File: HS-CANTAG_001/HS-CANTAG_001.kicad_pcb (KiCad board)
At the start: 2 copper layers, 81.3 x 52.1 mm, 28 parts, among them J1 B2B-PH-K-S_LF__SN_, J2 B4B-XH-A_LF__SN_, J3 Barrel_Jack, J4 CAN1, J5 CAN2, SW1 SW_Push, U1 MCP2515, U2 R-78E5.0-0.5, U3 MCP2551, Y1 16MHz

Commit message: ・回路修正
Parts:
- J4, J5: footprint Connector_Hirose:Hirose_DF63-4P-3.96DSA_1x04_P3.96mm_Horizontal -> Connector_JST:JST_VH_B4P-VH_1x04_P3.96mm_Vertical
- moved C1 77.4 mm to (134.5, 98.5)
- moved C2 77.4 mm to (156.1, 88.6)
- moved C3 77.4 mm to (149.8, 117.6)
- moved C4 77.4 mm to (159.9, 117.6)
- moved C5 77.4 mm to (172.6, 122.7)
- moved C6 77.4 mm to (123.1, 110.0)
- moved C7 77.4 mm to (130.7, 102.4)
- moved C8 77.4 mm to (130.7, 94.7)
- moved C9 77.4 mm to (123.1, 87.2)
- moved CAN_H1 77.4 mm to (170.1, 82.1)
- moved D1 77.4 mm to (162.5, 89.7)
- moved D2 77.4 mm to (132.0, 115.1)
- moved J1 77.4 mm to (132.0, 80.8)
- moved J2 77.4 mm to (142.0, 80.9)
- moved J3 77.4 mm to (120.6, 120.2)
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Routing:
- net Net-(U1-Pad1): track 0.00 -> 41.2 mm
- net Net-(U1-Pad2): track 0.00 -> 26.9 mm
- net +5V: track 225.2 -> 234.0 mm
- net Net-(CAN_H1-Pad2): track 69.7 -> 78.5 mm
- added copper zone on B.Cu, net GNDPWR
- added copper zone on F.Cu, net GNDPWR
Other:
- outline, holes or cut-outs redrawn

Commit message: ・CAN回路更新
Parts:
- U1: value MCP2515 -> MCP2515_SMD18p; footprint hotsprings-footprints:MCP2515_SMD -> hotsprings-footprints:MCP2515_SMD(18p)
- moved U1 1.28 mm to (154.9, 104.1)
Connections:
- U1 pad 10: GNDPWR -> Net-(U1-Pad10)
- U1 pad 11: Net-(U1-Pad11) -> Net-(D1-Pad2)
- U1 pad 12: Net-(D1-Pad2) -> Net-(U1-Pad12)
- U1 pad 13: Net-(U1-Pad13) -> Net-(J2-Pad1)
- U1 pad 14: Net-(J2-Pad1) -> Net-(J2-Pad2)
- U1 pad 15: Net-(U1-Pad15) -> Net-(J2-Pad3)
- U1 pad 16: Net-(J2-Pad2) -> Net-(J2-Pad4)
- U1 pad 17: Net-(J2-Pad3) -> Net-(R1-Pad2)
- U1 pad 18: Net-(J2-Pad4) -> +5V
- U1 pad 7: Net-(U1-Pad7) -> Net-(C3-Pad1)
- U1 pad 8: Net-(C3-Pad1) -> Net-(C4-Pad1)
- U1 pad 9: Net-(C4-Pad1) -> GNDPWR
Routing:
- net Net-(U1-Pad2): track 26.9 -> 33.0 mm
- net +5V: track 234.0 -> 229.3 mm
- net Net-(U1-Pad1): track 41.2 -> 37.3 mm
- net Net-(C3-Pad1): track 22.8 -> 20.2 mm
- net Net-(J2-Pad3): track 30.3 -> 28.1 mm
- net Net-(C4-Pad1): track 18.4 -> 16.3 mm
- net Net-(J2-Pad1): track 40.2 -> 38.3 mm
- net Net-(J2-Pad2): track 35.4 -> 33.5 mm
- net Net-(R1-Pad2): track 17.8 -> 16.0 mm
- net Net-(J2-Pad4): track 22.2 -> 20.9 mm
- net Net-(D1-Pad2): track 12.7 -> 11.5 mm

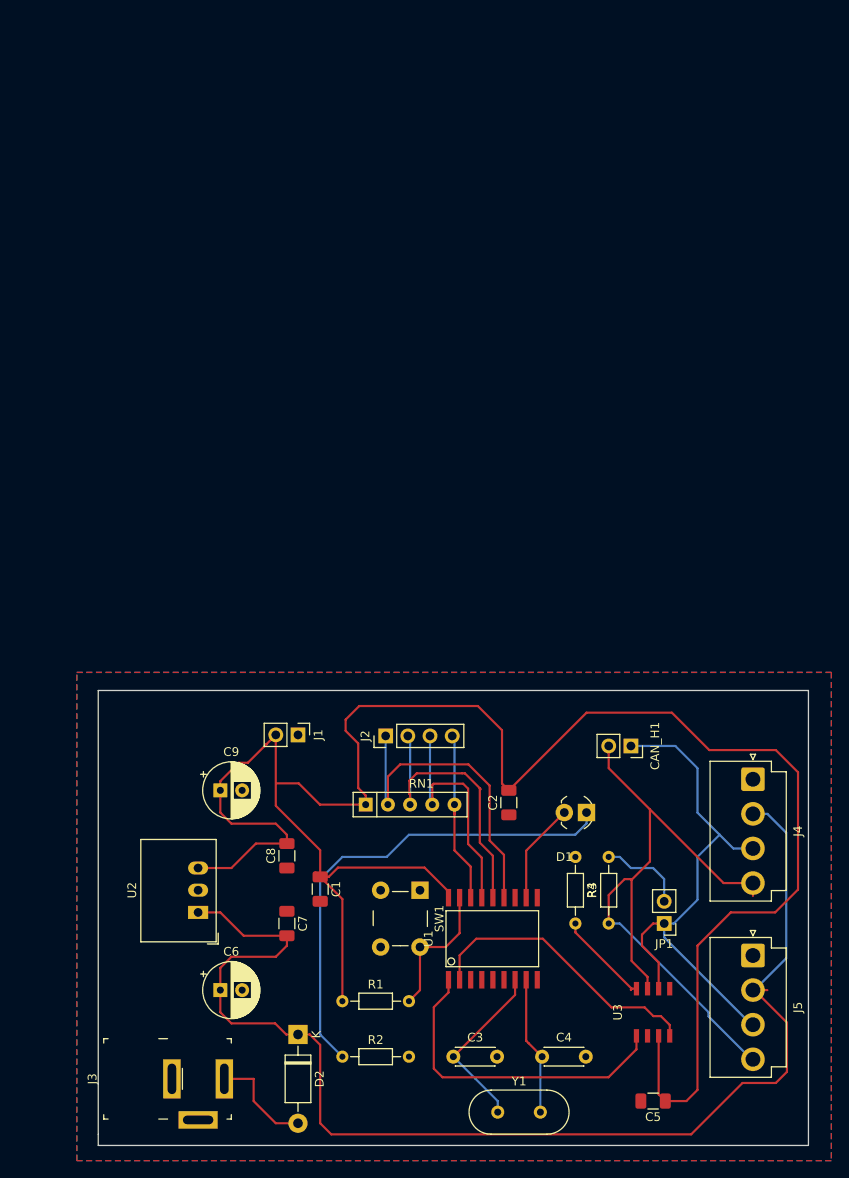
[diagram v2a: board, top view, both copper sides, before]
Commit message: ・CANTAG外形データの追加
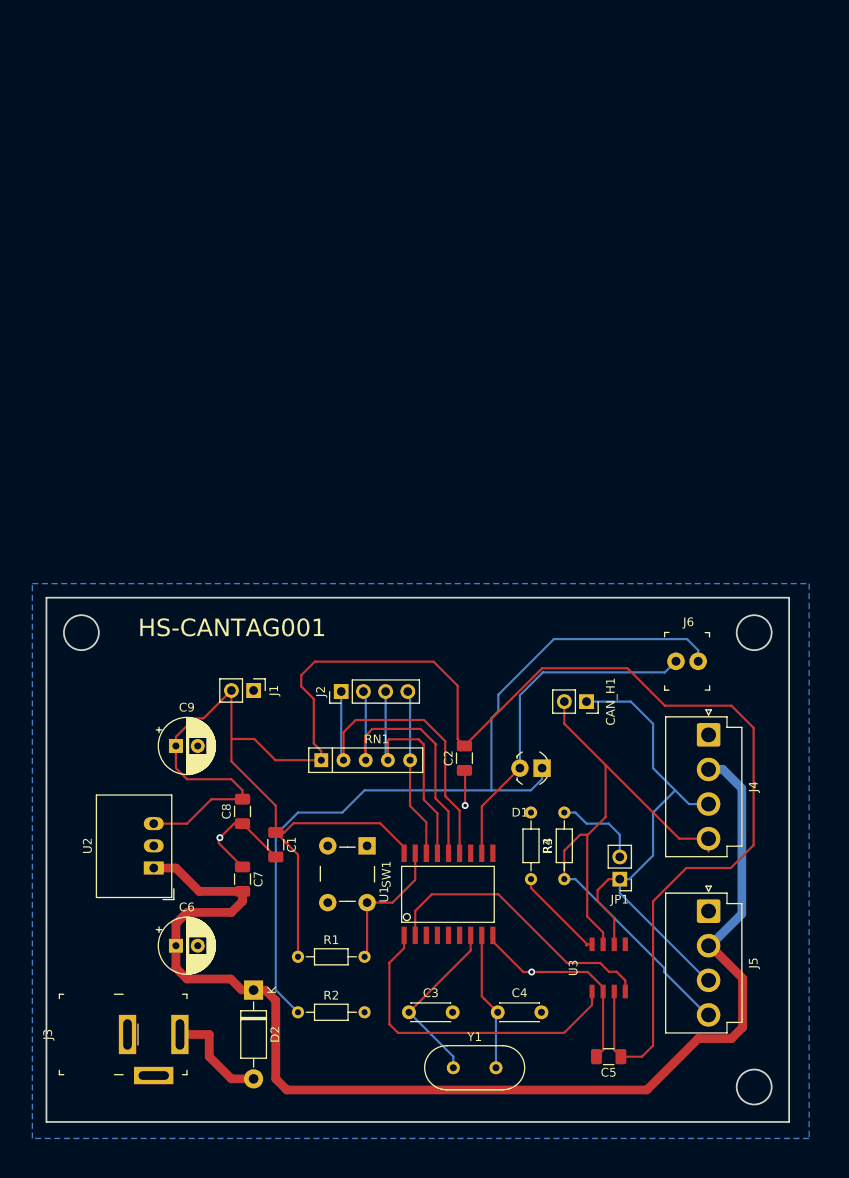
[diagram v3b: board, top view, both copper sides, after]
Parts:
- added J6: 640456-2, digikey-footprints:PinHeader_1x2_P2.54mm_Drill1.02mm, F.Cu at (175.3, 72.4)
- moved SW1 7.90 mm to (139.9, 93.5)
- moved J2 7.18 mm to (136.9, 75.8)
- moved R1 7.18 mm to (132.0, 106.2)
- moved R4 7.18 mm to (162.5, 97.3)
- moved RN1 7.18 mm to (134.7, 83.7)
- moved C3 7.18 mm to (144.7, 112.6)
- moved J3 7.18 mm to (115.5, 115.1)
- moved R2 7.18 mm to (132.0, 112.6)
- moved R3 7.18 mm to (158.7, 89.7)
- moved Y1 7.18 mm to (149.8, 118.9)
- moved C6 7.18 mm to (118.0, 104.9)
- moved C7 7.18 mm to (125.7, 97.3)
- moved C8 7.18 mm to (125.7, 89.6)
- moved C9 7.18 mm to (118.0, 82.1)
- moved D2 7.18 mm to (126.9, 110.0)
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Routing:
- net GNDPWR: track 0.00 -> 41.0 mm, vias 0 -> 3
- net Net-(D1-Pad1): track 55.7 -> 94.3 mm
- net Net-(D1-Pad2): track 11.5 -> 39.4 mm
- net VCC: track 142.1 -> 140.5 mm
- net Net-(R1-Pad2): track 16.0 -> 16.7 mm
- removed copper zone on F.Cu, net GNDPWR
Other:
- board size 81.3 x 52.1 mm -> 85 x 60 mm
- board text added: "HS-CANTAG001"

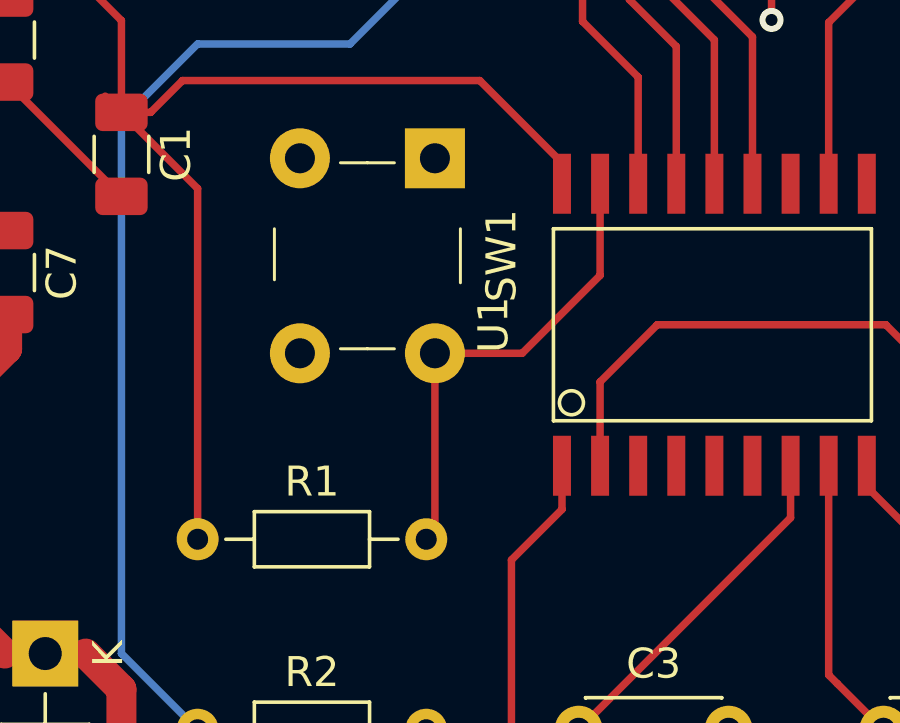
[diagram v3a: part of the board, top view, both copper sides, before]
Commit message: ・CANTAGボタン回路修正
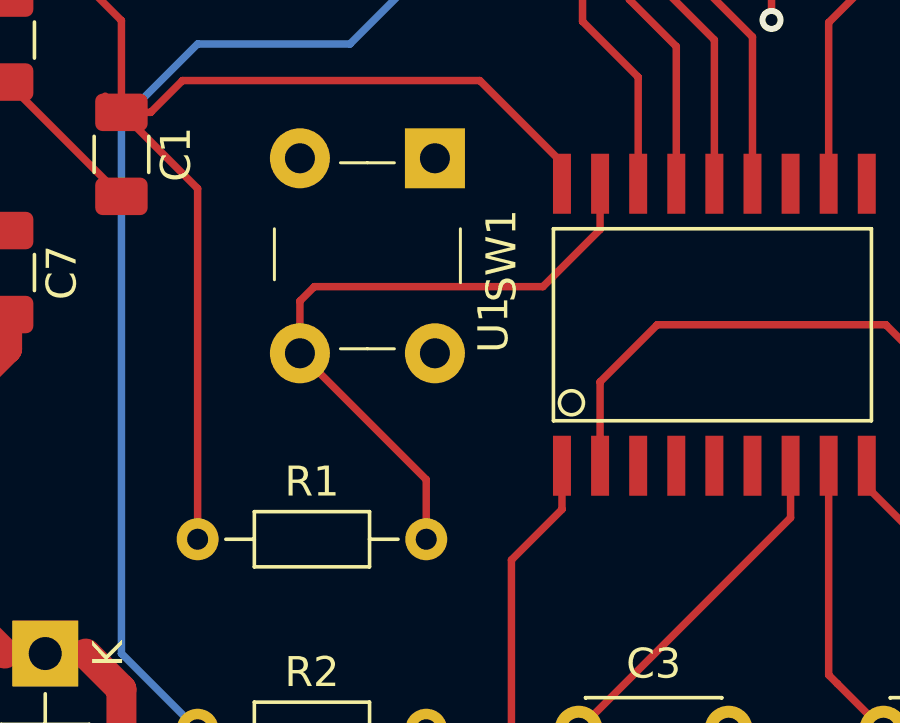
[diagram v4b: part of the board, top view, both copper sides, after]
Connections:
- SW1 pad 2: Net-(R1-Pad2) -> (no net)
- SW1 pad 4: (no net) -> Net-(R1-Pad2)
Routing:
- net Net-(R1-Pad2): track 16.7 -> 23.3 mm
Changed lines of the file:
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@@
     (thickness 1.6)
     (drawings 8)
-    (tracks 251)
+    (tracks 254)
     (zones 0)
     (modules 29)
@@
     (mod_text_size 1 1)
     (mod_text_width 0.15)
-    (pad_size 1.6 1.6)
-    (pad_drill 0.8)
+    (pad_size 2 2)
+    (pad_drill 1)
     (pad_to_mask_clearance 0.051)
     (solder_mask_min_width 0.25)
@@
     (pad 1 thru_hole rect (at 0.0012 0.0106 270) (size 2 2) (drill 1) (layers *.Cu *.Mask)
       (net 2 GNDPWR))
-    (pad 2 thru_hole circle (at 6.5012 0.0106 270) (size 2 2) (drill 1) (layers *.Cu *.Mask)
+    (pad 2 thru_hole circle (at 6.5012 0.0106 270) (size 2 2) (drill 1) (layers *.Cu *.Mask))
+    (pad 3 thru_hole circle (at 0.0012 4.5106 270) (size 2 2) (drill 1) (layers *.Cu *.Mask))
+    (pad 4 thru_hole circle (at 6.5012 4.5106 270) (size 2 2) (drill 1) (layers *.Cu *.Mask)
       (net 16 "Net-(R1-Pad2)"))
-    (pad 3 thru_hole circle (at 0.0012 4.5106 270) (size 2 2) (drill 1) (layers *.Cu *.Mask))
-    (pad 4 thru_hole circle (at 6.5012 4.5106 270) (size 2 2) (drill 1) (layers *.Cu *.Mask))
   )
   (module Converter_DCDC:Converter_DCDC_RECOM_R-78E-0.5_THT (layer F.Cu)
@@
   (gr_circle (center 107.210888 69.113241) (end 109.210888 69.113241) (layer Edge.Cuts) (width 0.2))
   (gr_line (start 188.210888 65.113241) (end 188.210888 125.113241) (layer Edge.Cuts) (width 0.2))
-  (via (at 151.13 88.9) (size 0.8) (drill 0.4) (layers F.Cu B.Cu) (net 2))
   (segment (start 122.1 88.17) (end 125.65 88.17) (width 0.25) (layer F.Cu) (net 1))
   (segment (start 119.3 90.97) (end 122.1 88.17) (width 0.25) (layer F.Cu) (net 1))
@@
   (segment (start 141.405 90.92) (end 131.495 90.92) (width 0.25) (layer F.Cu) (net 1))
   (segment (start 144.145 94.36) (end 144.145 93.66) (width 0.25) (layer F.Cu) (net 1))
+  (via (at 151.13 88.9) (size 0.8) (drill 0.4) (layers F.Cu B.Cu) (net 2))
   (segment (start 124.675 90.97) (end 123.0625 92.5825) (width 0.25) (layer F.Cu) (net 2))
   (segment (start 125.65 90.97) (end 124.675 90.97) (width 0.25) (layer F.Cu) (net 2))
@@
   (segment (start 145.415 94.36) (end 145.415 95.06) (width 0.25) (layer F.Cu) (net 16))
   (segment (start 139.9094 105.9206) (end 139.62 106.21) (width 0.25) (layer F.Cu) (net 16))
-  (segment (start 139.9094 100.0112) (end 139.9094 105.9206) (width 0.25) (layer F.Cu) (net 16))
-  (segment (start 145.415 94.36) (end 145.415 97.415) (width 0.25) (layer F.Cu) (net 16))
-  (segment (start 142.8188 100.0112) (end 139.9094 100.0112) (width 0.25) (layer F.Cu) (net 16))
-  (segment (start 145.415 97.415) (end 142.8188 100.0112) (width 0.25) (layer F.Cu) (net 16))
+  (segment (start 139.62 104.2218) (end 135.4094 100.0112) (width 0.25) (layer F.Cu) (net 16))
+  (segment (start 139.62 106.21) (end 139.62 104.2218) (width 0.25) (layer F.Cu) (net 16))
+  (segment (start 135.4094 100.0112) (end 135.4094 98.2706) (width 0.25) (layer F.Cu) (net 16))
+  (segment (start 135.4094 98.2706) (end 135.89 97.79) (width 0.25) (layer F.Cu) (net 16))
+  (segment (start 135.89 97.79) (end 143.51 97.79) (width 0.25) (layer F.Cu) (net 16))
+  (segment (start 145.415 95.885) (end 145.415 94.36) (width 0.25) (layer F.Cu) (net 16))
+  (segment (start 143.51 97.79) (end 145.415 95.885) (width 0.25) (layer F.Cu) (net 16))
   (segment (start 165.02 104.865) (end 165.105 104.78) (width 0.25) (layer F.Cu) (net 17))
   (segment (start 165.02 104.94) (end 165.02 104.865) (width 0.25) (layer F.Cu) (net 17))

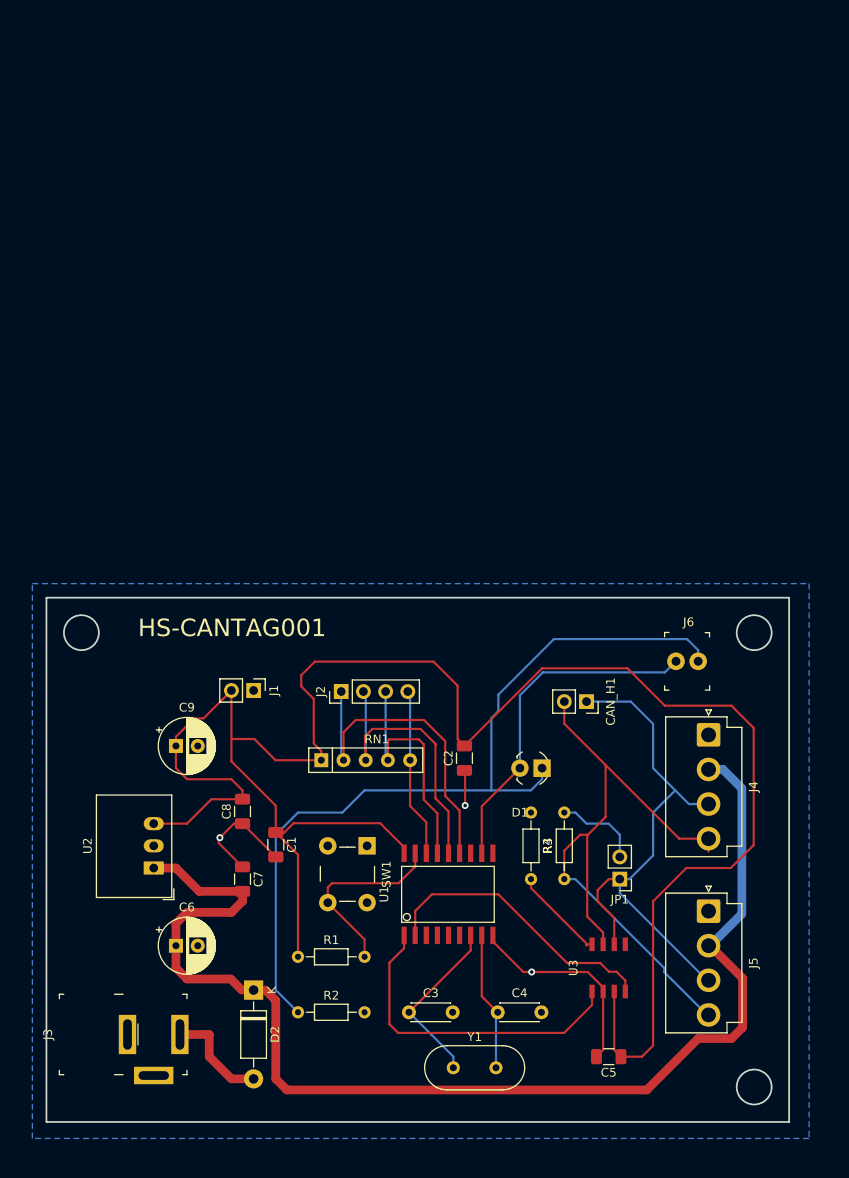
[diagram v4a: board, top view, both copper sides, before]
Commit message: ・CANTAG001外形変更 ・CANTAG002基盤修正
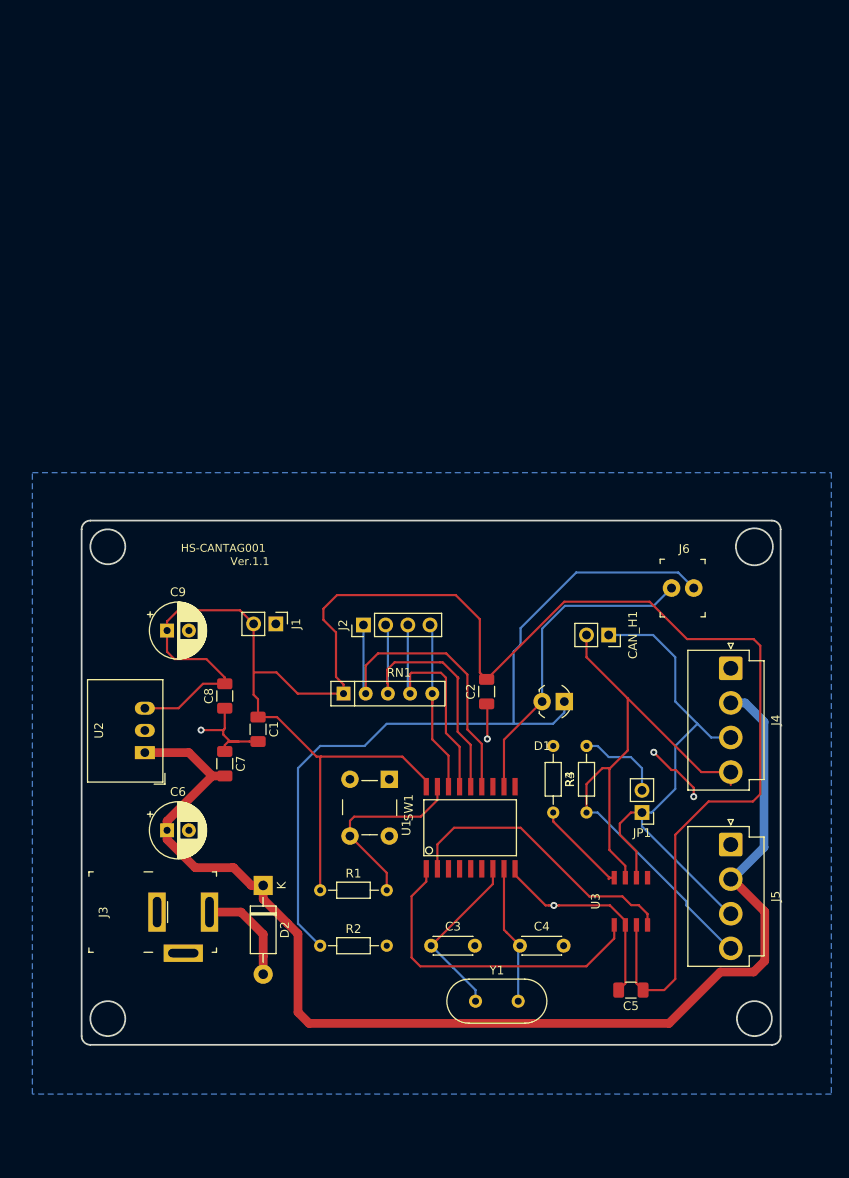
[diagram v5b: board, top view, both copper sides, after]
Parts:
- moved J3 14.4 mm to (118.9, 101.1)
- moved C1 13.4 mm to (127.4, 80.2)
- moved C7 13.4 mm to (123.6, 84.1)
- moved C8 13.4 mm to (123.6, 76.4)
- moved C6 13.2 mm to (117.0, 91.7)
- moved C9 13.2 mm to (117.0, 68.9)
- moved U2 13.2 mm to (114.5, 82.8)
- moved D2 12.0 mm to (128.0, 98.0)
- moved J6 8.40 mm to (174.8, 64.0)
- moved C3 8.03 mm to (147.2, 104.9)
- moved R3 8.03 mm to (161.2, 82.1)
- moved SW1 8.03 mm to (142.5, 85.9)
- moved J1 8.03 mm to (129.5, 68.1)
- moved C2 8.03 mm to (153.6, 75.9)
- moved C4 8.03 mm to (157.4, 104.9)
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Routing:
- net GNDPWR: track 41.0 -> 47.5 mm, vias 3 -> 5
- net Net-(D1-Pad1): track 94.3 -> 90.2 mm
- net +5V: track 229.3 -> 225.6 mm
- net Net-(D1-Pad2): track 39.4 -> 36.6 mm
- net VCC: track 140.5 -> 141.4 mm
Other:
- board size 85 x 60 mm -> 80 x 60 mm
- board text added: "Ver.1.1"
